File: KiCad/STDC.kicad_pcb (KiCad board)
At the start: 4 copper layers, 38 x 48 mm, 127 parts, among them IC1 TPS22916CNYFPR, IC2 TPS22916CNYFPR, IC3 R1200N001A-TR-FE, IC4 MS5849-30BA, IC5 W25Q32JWSNIQ, J1 TC2030, J2 S3B-PH-SM4-TB_LF__SN_, J3 Conn_01x34_NHD_18, Q1 AO3400A, Q2 AO3400A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

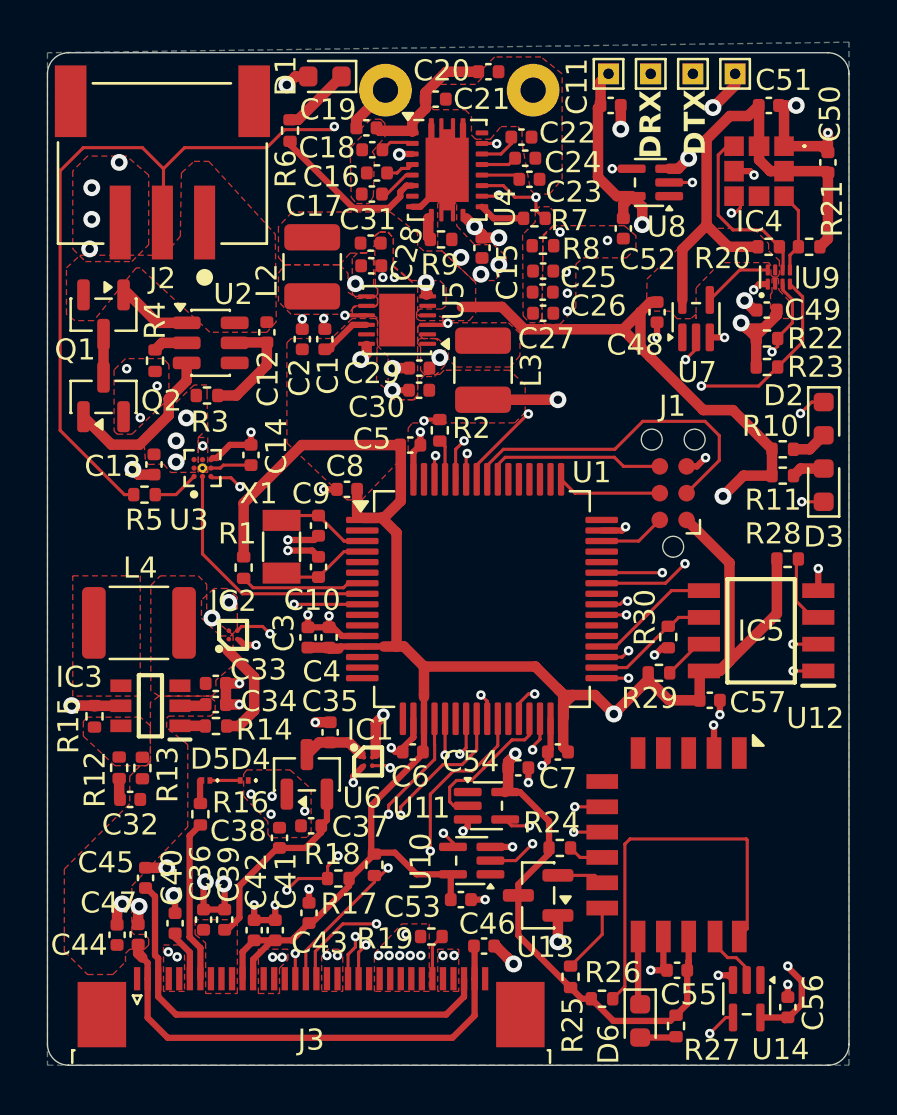
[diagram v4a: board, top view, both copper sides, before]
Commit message: Fewer GND cuts, 1.8V Routing for Pressure INT
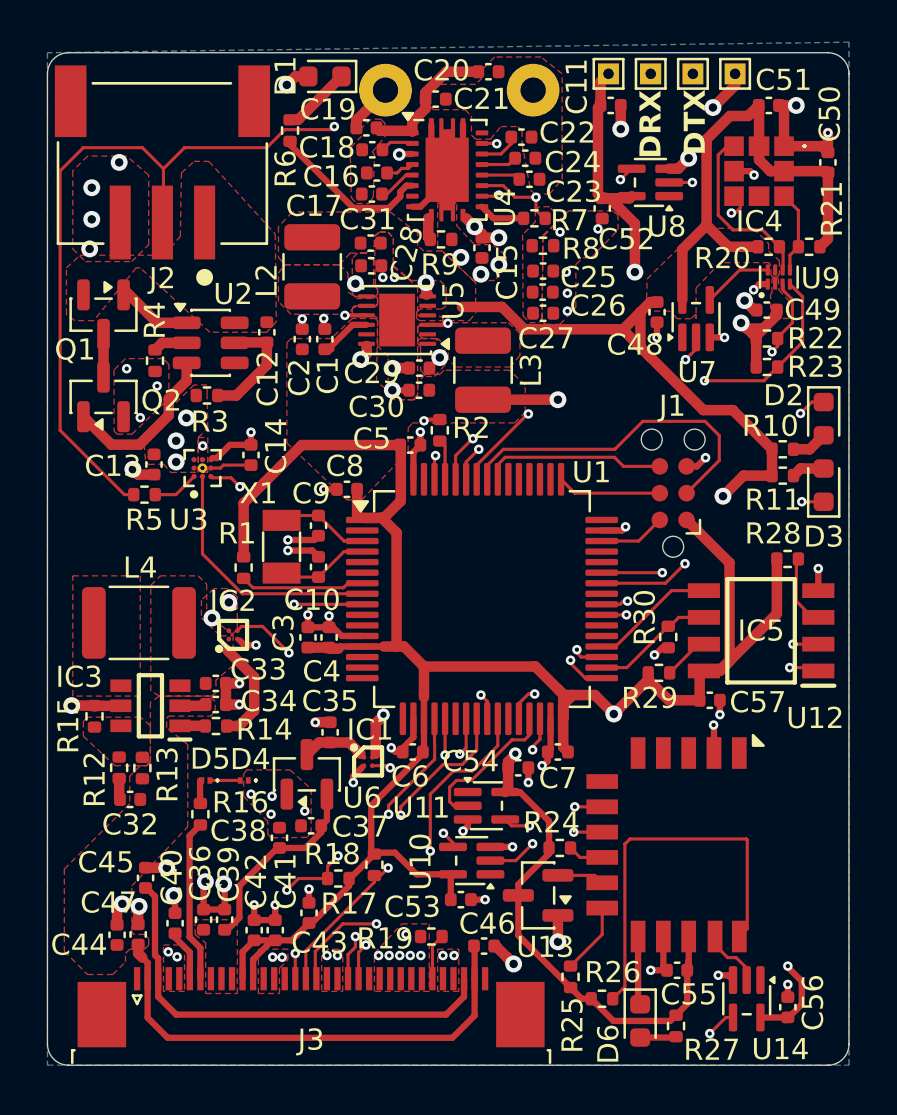
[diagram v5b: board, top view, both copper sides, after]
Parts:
- moved C52 1.38 mm to (151.3, 107.9)
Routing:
- net /SPI_NSS: track 10.4 -> 13.9 mm
- net /SPI_MISO: track 10.5 -> 13.0 mm
- net /Pressure Sensor/Pressure_INT: track 18.7 -> 17.8 mm
- net +1V8: track 153.3 -> 152.4 mm

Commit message: Move Connector down, fix silkscreen clearance errors, Stitching Vias for GND
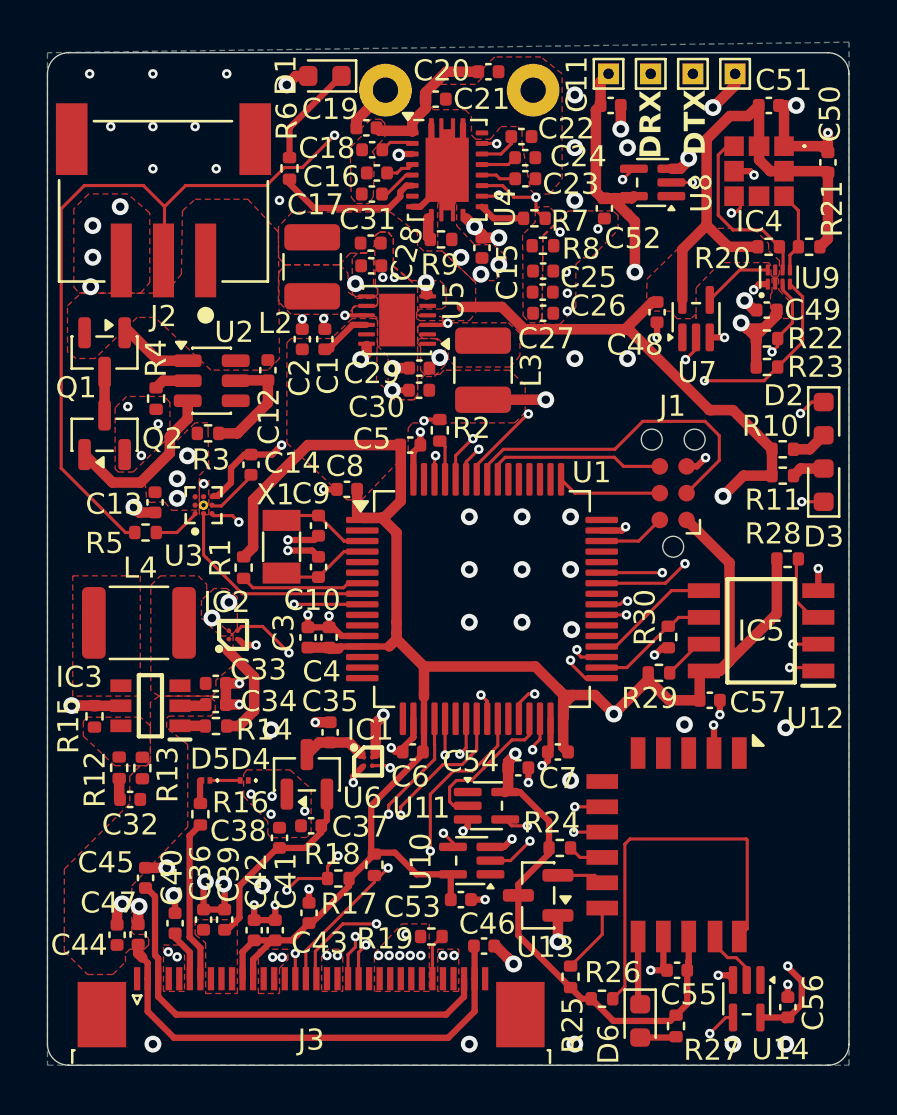
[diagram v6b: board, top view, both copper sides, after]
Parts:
- moved J2 1.80 mm to (130.5, 110.3)
- moved R3 1.80 mm to (132.6, 118.5)
- moved R4 1.80 mm to (130.2, 116.9)
- moved R5 1.80 mm to (129.7, 123.2)
- moved Q1 1.80 mm to (127.7, 114.7)
- moved Q2 1.80 mm to (127.7, 118.6)
- moved C12 1.80 mm to (135.4, 115.5)
- moved C13 1.80 mm to (130.1, 121.8)
- moved U2 1.80 mm to (132.8, 116.0)
- moved R6 1.80 mm to (136.5, 106.0)
- moved U3 1.76 mm to (132.4, 122.0)
- moved C14 0.46 mm to (134.7, 120.0)
- moved C23 0.20 mm to (147.7, 106.5)
- moved C52 0.10 mm to (151.4, 107.9)
- moved U8 0.10 mm to (153.7, 106.7)
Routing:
- net +3.3V: track 102.5 -> 99.1 mm
- net GND: track 79.1 -> 81.4 mm, vias 88 -> 122
- net /Power+Battery/Batt_Status_SDA: track 11.9 -> 10.0 mm
- net /Power+Battery/Batt_Status_SCL: track 11.9 -> 10.1 mm
- net /Power+Battery//CH_RES: track 3.38 -> 5.10 mm
- net /Power+Battery//CHARGE: track 7.94 -> 7.14 mm
- net /Power+Battery/TS_CTRL: track 45.5 -> 46.1 mm
- net /Power+Battery/Stat_REG: track 1.86 -> 2.40 mm
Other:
- board text added: "Sebastian Thomas 04/2026"
- board text added: "{ "ViaStitching": "0.2", "stitch_zone_0": { "HSpacing": "2.5", "VSpacing": "2.5", "HOffset": "0", "VOffset": "0", "Clearance": "0", "Randomize": false } }"
- board text removed: "Sebastian Thomas 03/2026"

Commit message: Generate output files with 0 mask expansion
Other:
- rule pad_to_mask_clearance: 0.05 -> 0
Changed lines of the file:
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@@
 			(dielectric_constraints no)
 		)
-		(pad_to_mask_clearance 0.05)
+		(pad_to_mask_clearance 0)
 		(allow_soldermask_bridges_in_footprints no)
 		(tenting front back)
